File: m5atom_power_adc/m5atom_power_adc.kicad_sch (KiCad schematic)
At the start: 123 parts, among them J10 Conn_01x02, J11 Conn_01x02, J12 Conn_01x02, J13 Conn_01x02, J14 Conn_01x02, J2 GROVE-CONNECTOR, J3 Conn_01x04_Pin, J4 USB_C_Receptacle_USB2.0_16P, J5 SubBatt, J6 MainBatt, J7 Conn_01x02, J8 Conn_01x02, J9 GROVE-CONNECTOR, Q1 AO3401A, Q2 MMBT2222A, Q3 MMBT2222A, Q4 MMBT2222A, Q5 AO3401A, Q6 MMBT2222A, Q7 MMBT2222A, Q8 AO3401A, Q9 MMBT2222A, SW1 Boot, SW2 Reset, U1 LM2596S-5, U2 ESP32-S3-MINI-1, U3 AMS1117-3.3, U4 ADS1115IDGS, U5 AMS1117-3.3, U6 LTC2944

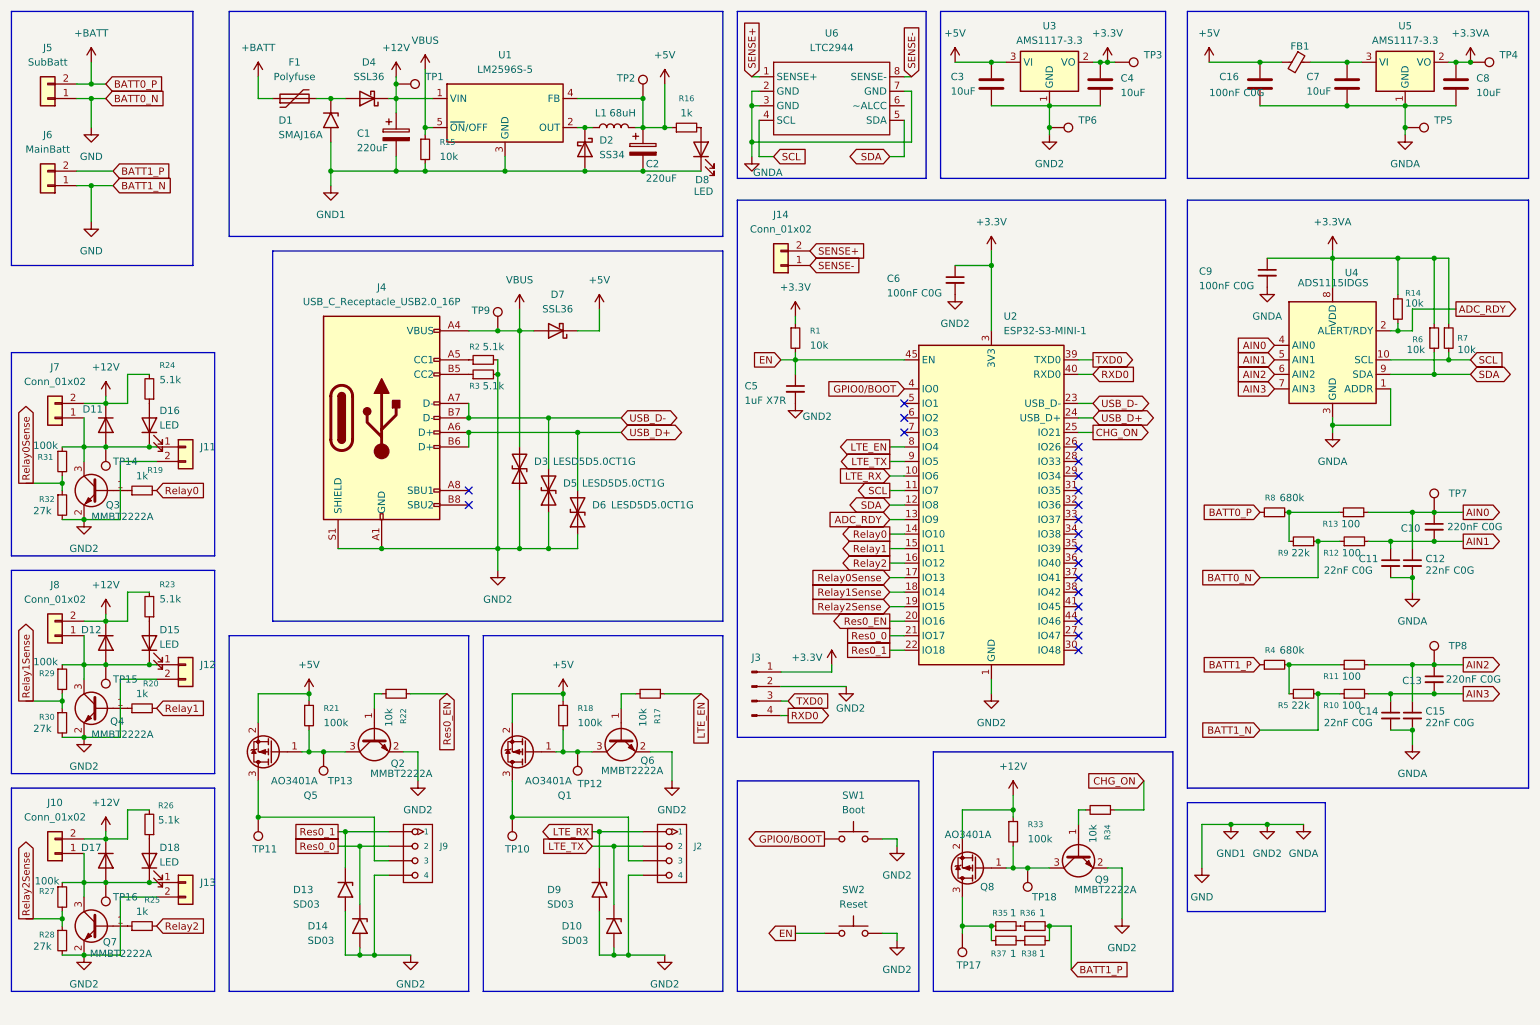
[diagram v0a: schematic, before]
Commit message: chore: 回路図更新・カスタムフットプリント追加
- USB-C受電回路（CC1/CC2プルダウン、ESD保護、ORダイオード）追加
- リレーコイルセンシング回路追加（100k+27k分圧）
- 電源インジケーターLED（D8）を+5Vラインから取るよう変更
- リレー制御BJTベース抵抗を10kΩ→1kΩに修正
- Groveコネクタ・インダクタのカスタムフットプリント追加
- フットプリントライブラリテーブル追加

Co-Authored-By: Claude Sonnet 4.6 <noreply@anthropic.com>
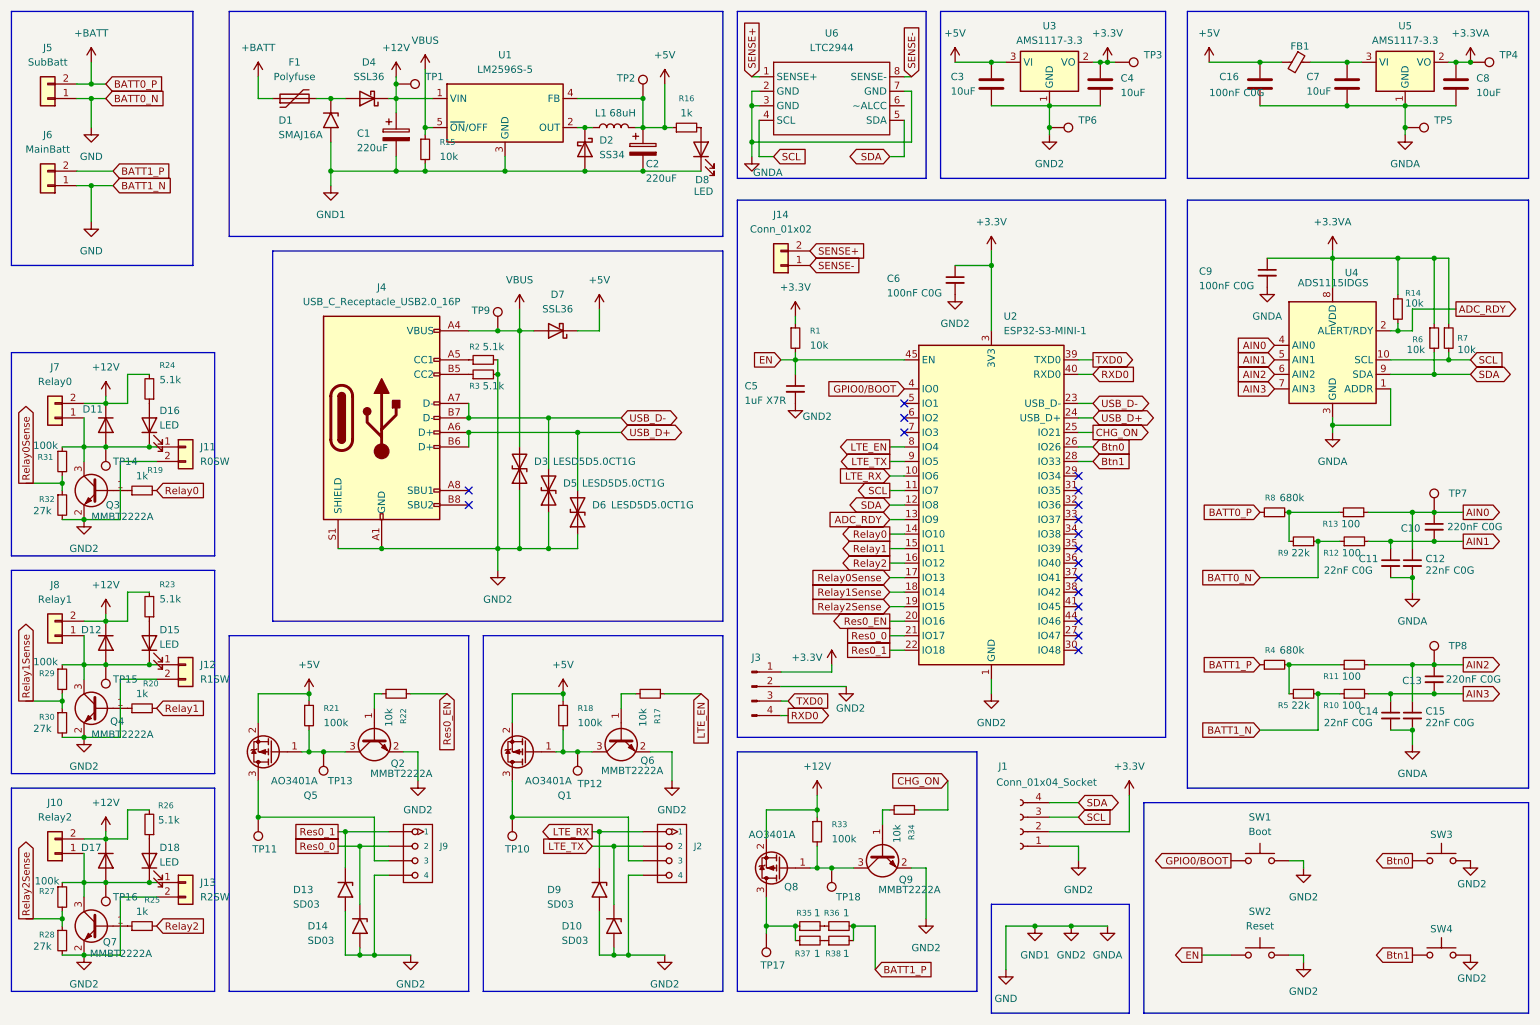
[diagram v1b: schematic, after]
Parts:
- added J1: Conn_01x04_Socket, Connector_JST:JST_XH_S4B-XH-SM4-TB_1x04-1MP_P2.50mm_Horizontal, symbol Connector:Conn_01x04_Socket
- added SW3, SW4: ~, symbol Switch:SW_Push
- J10: value Conn_01x02 -> Relay2; footprint (none) -> Connector_JST:JST_XH_B2B-XH-A_1x02_P2.50mm_Vertical; JLC_Num (none) -> C158012
- J11: value Conn_01x02 -> R0SW; footprint (none) -> Connector_JST:JST_XH_B2B-XH-A_1x02_P2.50mm_Vertical; JLC_Num (none) -> C158012
- J12: value Conn_01x02 -> R1SW; footprint (none) -> Connector_JST:JST_XH_B2B-XH-A_1x02_P2.50mm_Vertical; JLC_Num (none) -> C158012
- J13: value Conn_01x02 -> R2SW; footprint (none) -> Connector_JST:JST_XH_B2B-XH-A_1x02_P2.50mm_Vertical; JLC_Num (none) -> C158012
- J14, J5, J6: footprint (none) -> Connector_JST:JST_XH_B2B-XH-A_1x02_P2.50mm_Vertical; JLC_Num (none) -> C158012
- J2, J9: footprint (none) -> 000_Local:HY2.0-4PWB; JLC_Num (none) -> C3029460
- J3: footprint (none) -> Connector_PinHeader_2.54mm:PinHeader_1x04_P2.54mm_Vertical
- J7: value Conn_01x02 -> Relay0; footprint (none) -> Connector_JST:JST_XH_B2B-XH-A_1x02_P2.50mm_Vertical; JLC_Num (none) -> C158012
- J8: value Conn_01x02 -> Relay1; footprint (none) -> Connector_JST:JST_XH_B2B-XH-A_1x02_P2.50mm_Vertical; JLC_Num (none) -> C158012
- L1: footprint (none) -> 000_Local:PSPMAA0605H-680M-IGF; JLC_Num (none) -> C2983094
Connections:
- net +3.3V: now also J1.2 (Pin_2)
- net GND: now also J1.1 (Pin_1), SW3.2, SW4.2
- net SCL: now also J1.3 (Pin_3)
- net SDA: now also J1.4 (Pin_4)
- net Btn0: now reaches U2.26 (IO26)
- net Btn0: now also SW3.1
- net Btn1: now reaches U2.28 (IO33)
- net Btn1: now also SW4.1
- no-connect marks 20 -> 18
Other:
- moved on the sheet: Q8, Q9, R33, R34, R35, R36, R37, R38, SW1, SW2, TP17, TP18
